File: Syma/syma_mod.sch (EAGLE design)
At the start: 6 parts, among them Q1 BSS84, Q2 BSS84, Q3 BSS84

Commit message: syma update
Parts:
- added C1: 470p, rcl:C-EUC0603
- added D1: (no value), palmquad_alpha:DIODE-MINIMELF
- added M4: MOTORARM-CORNER, palmquad_alpha:MOTORARM-CORNER
- added Q5: DMN2075U, palmquad_alpha:MOSFET-NCHANNELSMD
- added R7: 680K, rcl:R-US_R0603
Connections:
- new net GND: Q5.S, R7.1
- new net N$20: D1.A, M4.2, Q5.D
- new net N$45: C1.2, Q5.G
- new net OC3A: C1.1, R7.2
- new net VBATT: D1.C, M4.1
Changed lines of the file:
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@@
 <layer number="48" name="Document" color="7" fill="1" visible="no" active="no"/>
 <layer number="49" name="Reference" color="7" fill="1" visible="no" active="no"/>
+<layer number="50" name="dxf" color="7" fill="1" visible="no" active="no"/>
 <layer number="51" name="tDocu" color="7" fill="1" visible="no" active="no"/>
 <layer number="52" name="bDocu" color="7" fill="1" visible="no" active="no"/>
+<layer number="53" name="tGND_GNDA" color="7" fill="9" visible="no" active="no"/>
+<layer number="54" name="bGND_GNDA" color="1" fill="9" visible="no" active="no"/>
+<layer number="56" name="wert" color="7" fill="1" visible="no" active="no"/>
 <layer number="90" name="Modules" color="5" fill="1" visible="yes" active="yes"/>
 <layer number="91" name="Nets" color="2" fill="1" visible="yes" active="yes"/>
@@
 <layer number="97" name="Info" color="7" fill="1" visible="yes" active="yes"/>
 <layer number="98" name="Guide" color="6" fill="1" visible="yes" active="yes"/>
+<layer number="100" name="Muster" color="7" fill="1" visible="no" active="no"/>
+<layer number="101" name="Patch_Top" color="12" fill="4" visible="yes" active="yes"/>
+<layer number="102" name="Vscore" color="7" fill="1" visible="yes" active="yes"/>
+<layer number="103" name="tMap" color="7" fill="1" visible="yes" active="yes"/>
+<layer number="104" name="Name" color="16" fill="1" visible="yes" active="yes"/>
+<layer number="105" name="tPlate" color="7" fill="1" visible="yes" active="yes"/>
+<layer number="106" name="bPlate" color="7" fill="1" visible="yes" active="yes"/>
+<layer number="107" name="Crop" color="7" fill="1" visible="yes" active="yes"/>
+<layer number="116" name="Patch_BOT" color="9" fill="4" visible="yes" active="yes"/>
+<layer number="121" name="_tsilk" color="7" fill="1" visible="yes" active="yes"/>
+<layer number="122" name="_bsilk" color="7" fill="1" visible="yes" active="yes"/>
+<layer number="125" name="_tNames" color="7" fill="1" visible="no" active="yes"/>
+<layer number="144" name="Drill_legend" color="7" fill="1" visible="no" active="yes"/>
+<layer number="151" name="HeatSink" color="7" fill="1" visible="yes" active="yes"/>
+<layer number="200" name="200bmp" color="1" fill="10" visible="yes" active="yes"/>
+<layer number="201" name="201bmp" color="2" fill="10" visible="yes" active="yes"/>
+<layer number="202" name="202bmp" color="3" fill="10" visible="yes" active="yes"/>
+<layer number="203" name="203bmp" color="4" fill="10" visible="yes" active="yes"/>
+<layer number="204" name="204bmp" color="5" fill="10" visible="yes" active="yes"/>
+<layer number="205" name="205bmp" color="6" fill="10" visible="yes" active="yes"/>
+<layer number="206" name="206bmp" color="7" fill="10" visible="yes" active="yes"/>
+<layer number="207" name="207bmp" color="8" fill="10" visible="yes" active="yes"/>
+<layer number="208" name="208bmp" color="9" fill="10" visible="yes" active="yes"/>
+<layer number="209" name="209bmp" color="7" fill="1" visible="yes" active="yes"/>
+<layer number="210" name="210bmp" color="7" fill="1" visible="yes" active="yes"/>
+<layer number="211" name="211bmp" color="7" fill="1" visible="yes" active="yes"/>
+<layer number="212" name="212bmp" color="7" fill="1" visible="yes" active="yes"/>
+<layer number="213" name="213bmp" color="7" fill="1" visible="yes" active="yes"/>
+<layer number="214" name="214bmp" color="7" fill="1" visible="yes" active="yes"/>
+<layer number="215" name="215bmp" color="7" fill="1" visible="yes" active="yes"/>
+<layer number="216" name="216bmp" color="7" fill="1" visible="yes" active="yes"/>
+<layer number="217" name="217bmp" color="7" fill="1" visible="yes" active="yes"/>
+<layer number="218" name="218bmp" color="7" fill="1" visible="yes" active="yes"/>
+<layer number="219" name="219bmp" color="7" fill="1" visible="yes" active="yes"/>
+<layer number="220" name="220bmp" color="7" fill="1" visible="yes" active="yes"/>
+<layer number="221" name="221bmp" color="7" fill="1" visible="yes" active="yes"/>
+<layer number="222" name="222bmp" color="7" fill="1" visible="yes" active="yes"/>
+<layer number="223" name="223bmp" color="7" fill="1" visible="yes" active="yes"/>
+<layer number="224" name="224bmp" color="7" fill="1" visible="yes" active="yes"/>
+<layer number="250" name="Descript" color="3" fill="1" visible="no" active="no"/>
+<layer number="251" name="SMDround" color="12" fill="11" visible="no" active="no"/>
+<layer number="254" name="cooling" color="7" fill="1" visible="yes" active="yes"/>
 </layers>
 <schematic xreflabel="%F%N/%S.%C%R" xrefpart="/%S.%C%R">
@@
 </part>
 <part name="SUPPLY1" library="supply2" deviceset="GND" device=""/>
+<part name="M4" library="palmquad_alpha" deviceset="MOTOR" device="ARM-CORNER"/>
+<part name="Q5" library="palmquad_alpha" deviceset="MOSFET-NCHANNEL" device="SMD" value="DMN2075U"/>
+<part name="R7" library="rcl" deviceset="R-US_" device="R0603" value="680K"/>
+<part name="GND20" library="supply1" deviceset="GND" device=""/>
+<part name="SUPPLY8" library="supply2" deviceset="+5V" device="" value="Vbatt"/>
+<part name="D1" library="palmquad_alpha" deviceset="DIODE-" device="MINIMELF"/>
+<part name="C1" library="rcl" deviceset="C-EU" device="C0603" value="470p"/>
 </parts>
 <sheets>
@@
 </instance>
 <instance part="SUPPLY1" gate="GND" x="114.3" y="180.34"/>
+<instance part="M4" gate="G$1" x="83.82" y="83.82" rot="R270"/>
+<instance part="Q5" gate="G$1" x="83.82" y="66.04"/>
+<instance part="R7" gate="G$1" x="60.96" y="58.42" rot="R90"/>
+<instance part="GND20" gate="1" x="83.82" y="45.72"/>
+<instance part="SUPPLY8" gate="+5V" x="83.82" y="99.06"/>
+<instance part="D1" gate="G$1" x="91.44" y="83.82" rot="R90"/>
+<instance part="C1" gate="G$1" x="66.04" y="66.04" rot="R90"/>
 </instances>
 <busses>
@@
 <pinref part="SUPPLY1" gate="GND" pin="GND"/>
 </segment>
+<segment>
+<wire x1="83.82" y1="60.96" x2="83.82" y2="50.8" width="0.1524" layer="91"/>
+<wire x1="83.82" y1="50.8" x2="83.82" y2="48.26" width="0.1524" layer="91"/>
+<wire x1="60.96" y1="53.34" x2="60.96" y2="50.8" width="0.1524" layer="91"/>
+<wire x1="60.96" y1="50.8" x2="83.82" y2="50.8" width="0.1524" layer="91"/>
+<pinref part="Q5" gate="G$1" pin="S"/>
+<pinref part="GND20" gate="1" pin="GND"/>
+<pinref part="R7" gate="G$1" pin="1"/>
+</segment>
 </net>
 <net name="N$1" class="0">
@@
 </segment>
 </net>
+<net name="N$20" class="0">
+<segment>
+<wire x1="83.82" y1="73.66" x2="83.82" y2="71.12" width="0.1524" layer="91"/>
+<wire x1="83.82" y1="73.406" x2="83.82" y2="73.66" width="0.1524" layer="91"/>
+<wire x1="91.44" y1="81.28" x2="91.44" y2="73.406" width="0.1524" layer="91"/>
+<wire x1="91.44" y1="73.406" x2="83.82" y2="73.406" width="0.1524" layer="91"/>
+<pinref part="Q5" gate="G$1" pin="D"/>
+<pinref part="M4" gate="G$1" pin="2"/>
+<pinref part="D1" gate="G$1" pin="A"/>
+</segment>
+</net>
+<net name="OC3A" class="0">
+<segment>
+<wire x1="60.96" y1="66.04" x2="60.96" y2="63.5" width="0.1524" layer="91"/>
+<wire x1="60.96" y1="66.04" x2="50.8" y2="66.04" width="0.1524" layer="91"/>
+<wire x1="60.96" y1="66.04" x2="63.5" y2="66.04" width="0.1524" layer="91"/>
+<label x="53.34" y="66.04" size="1.778" layer="95"/>
+<pinref part="R7" gate="G$1" pin="2"/>
+<pinref part="C1" gate="G$1" pin="1"/>
+</segment>
+</net>
+<net name="VBATT" class="0">
+<segment>
+<wire x1="83.82" y1="96.52" x2="83.82" y2="94.234" width="0.1524" layer="91"/>
+<wire x1="83.82" y1="94.234" x2="83.82" y2="93.98" width="0.1524" layer="91"/>
+<wire x1="91.44" y1="86.36" x2="91.44" y2="94.234" width="0.1524" layer="91"/>
+<wire x1="91.44" y1="94.234" x2="83.82" y2="94.234" width="0.1524" layer="91"/>
+<pinref part="SUPPLY8" gate="+5V" pin="+5V"/>
+<pinref part="M4" gate="G$1" pin="1"/>
+<pinref part="D1" gate="G$1" pin="C"/>
+</segment>
+</net>
+<net name="N$45" class="0">
+<segment>
+<wire x1="71.12" y1="66.04" x2="76.2" y2="66.04" width="0.1524" layer="91"/>
+<pinref part="Q5" gate="G$1" pin="G"/>
+<pinref part="C1" gate="G$1" pin="2"/>
+</segment>
+</net>

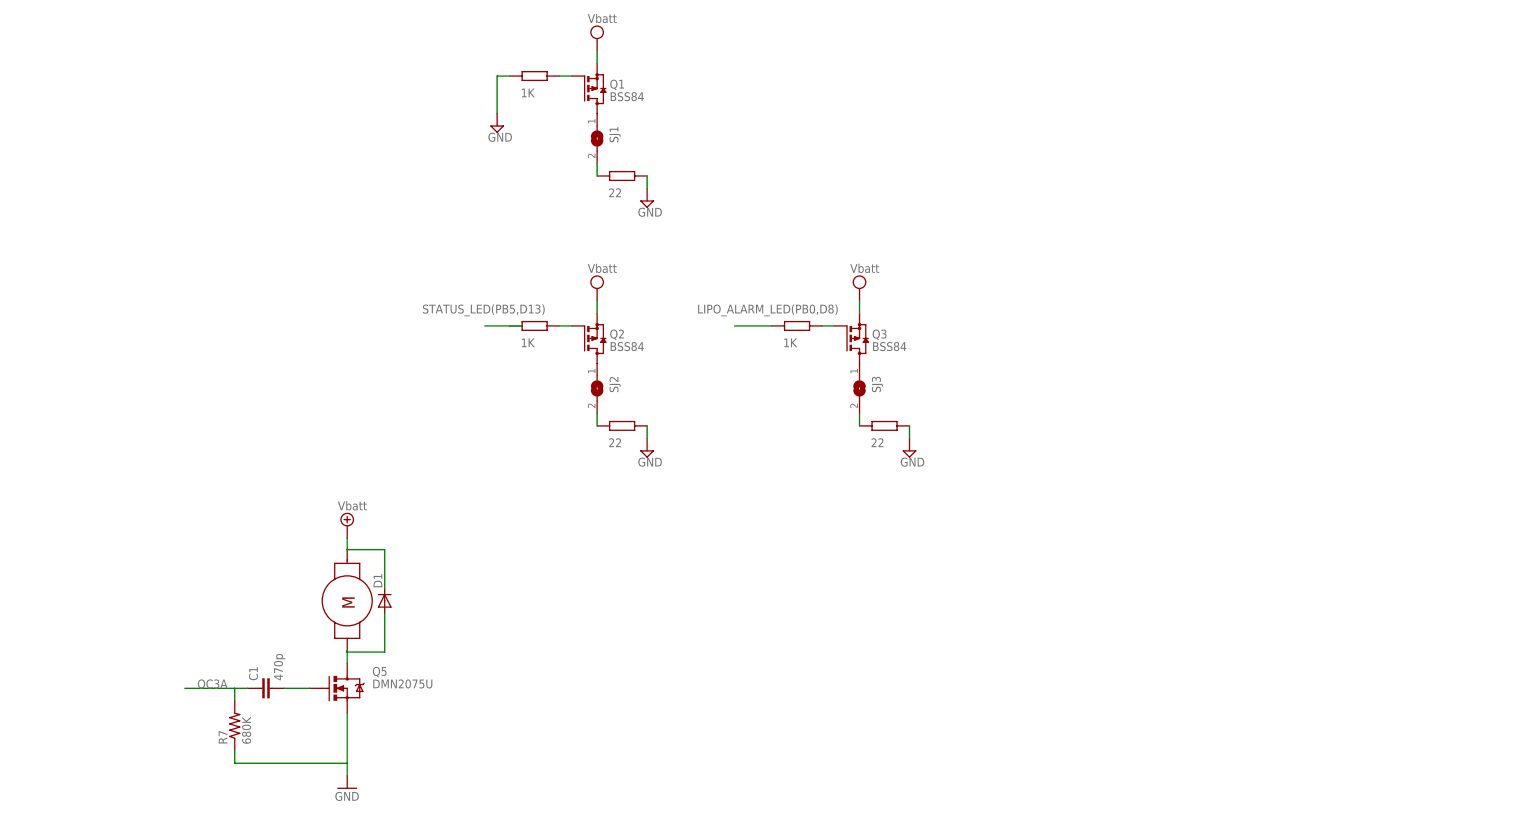
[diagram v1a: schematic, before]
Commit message: syma schematic updated
avr is added
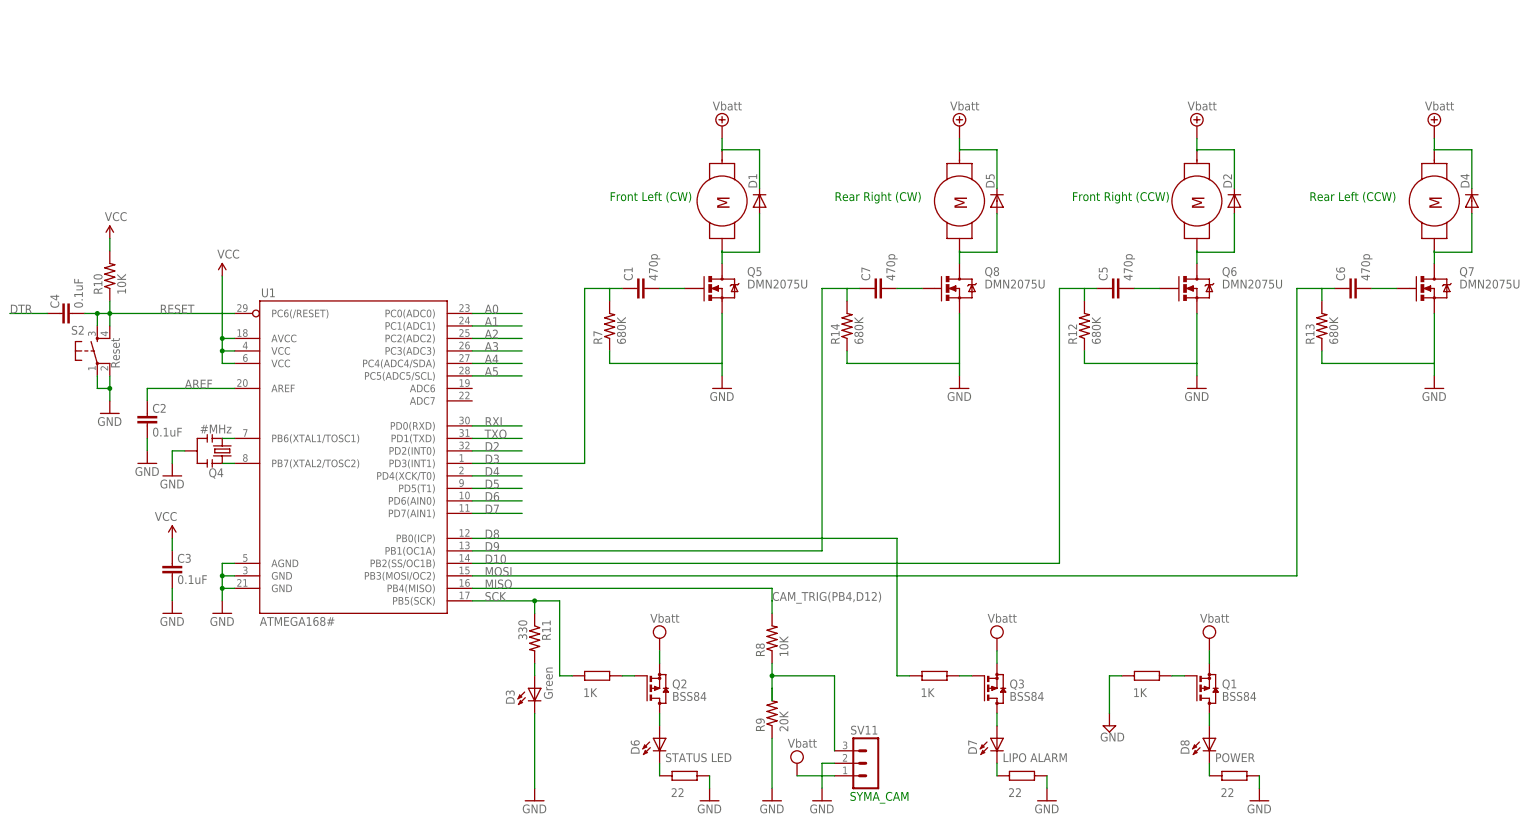
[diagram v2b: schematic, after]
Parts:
- removed SJ1, SJ2, SJ3: (no value), jumper:SJW
- added C2, C3, C4: 0.1uF, SparkFun:CAP0402
- added C5, C6, C7: 470p, rcl:C-EUC0603
- added D2, D4, D5: (no value), palmquad_alpha:DIODE-MINIMELF
- added D3: Green, SparkFun:LED0603
- added D6: STATUS LED, SparkFun:LED0603
- added D7: LIPO ALARM, SparkFun:LED0603
- added D8: POWER, SparkFun:LED0603
- added M1, M2, M3: MOTORARM-CORNER, palmquad_alpha:MOTORARM-CORNER
- added Q4: #MHz, SparkFun:RESONATORSMD
- added Q6, Q7, Q8: DMN2075U, palmquad_alpha:MOSFET-NCHANNELSMD
- added R10: 10K, SparkFun:RESISTOR0402
- added R11: 330, SparkFun:RESISTOR0402
- added R12, R13, R14: 680K, rcl:R-US_R0603
- added R8: 10K, rcl:R-US_R0603
- added R9: 20K, rcl:R-US_R0603
- added S2: Reset, SparkFun:TAC_SWITCHSND
- added SV11: (no value), con-lstb:MA03-1
- added U1: ATMEGA168#, SparkFun:ATMEGA168
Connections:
- removed net OC3A: C1.1, R7.2
- new net A0: U1.PC0(ADC0)
- new net A1: U1.PC1(ADC1)
- new net A2: U1.PC2(ADC2)
- new net A3: U1.PC3(ADC3)
- new net A4: U1.PC4(ADC4/SDA)
- new net A5: U1.PC5(ADC5/SCL)
- new net AREF: C2.2, U1.AREF
- new net CAM_TRIG(PB4,D12): R8.2
- new net D10: C5.1, R12.2, U1.PB2(SS/OC1B)
- new net D2: U1.PD2(INT0)
- new net D3: C1.1, R7.2, U1.PD3(INT1)
- new net D4: U1.PD4(XCK/T0)
- new net D5: U1.PD5(T1)
- new net D6: U1.PD6(AIN0)
- new net D7: U1.PD7(AIN1)
- new net D8: U1.PB0(ICP)
- new net D9: C7.1, R14.2, U1.PB1(OC1A)
- new net DTR: C4.2
- new net MISO: U1.PB4(MISO)
- new net MOSI: C6.1, R13.2, U1.PB3(MOSI/OC2)
- new net N$10: D3.A, R11.2
- new net N$11: Q4.1, U1.PB7(XTAL2/TOSC2)
- new net N$12: Q4.3, U1.PB6(XTAL1/TOSC1)
- new net N$13: D2.A, M1.2, Q6.D
- new net N$14: C5.2, Q6.G
- new net N$15: D4.A, M2.2, Q7.D
- new net N$16: C6.2, Q7.G
- new net N$17: D5.A, M3.2, Q8.D
- new net N$18: C7.2, Q8.G
- new net RESET: C4.1, R10.1, S2.3, S2.4, U1.PC6(/RESET)
- new net RXI: U1.PD0(RXD)
- new net SCK: R11.1, U1.PB5(SCK)
- new net SYMA_CAM_TRIG: R8.1, R9.2, SV11.3
- new net TXO: U1.PD1(TXD)
- net GND: now also C2.1, C3.1, D3.C, Q4.2, Q6.S, Q7.S, Q8.S, R12.1, R13.1, R14.1, R9.1, S2.1, S2.2, SV11.2, U1.AGND, U1.GND@1, U1.GND@2
- net N$1: now also D6.A; no longer SJ2.1
- net N$2: now also D6.C; no longer SJ2.2
- net N$4: now also D7.A; no longer SJ3.1
- net N$5: now also D7.C; no longer SJ3.2
- net N$7: now also D8.A; no longer SJ1.1
- net N$8: now also D8.C; no longer SJ1.2
- net VBATT: now also D2.C, D4.C, D5.C, M1.1, M2.1, M3.1
- net VCC: now also C3.2, R10.2, SV11.1, U1.AVCC, U1.VCC@1, U1.VCC@2
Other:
- note added: "Front Left (CW)"
- note added: "Front Right (CCW)"
- note added: "Rear Left (CCW)"
- note added: "Rear Right (CW)"
- note added: "SYMA_CAM"
- moved on the sheet: C1, D1, Q1, Q2, Q3, Q5, R7

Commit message: syma schematic - add voltage sense
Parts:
- added R15, R16: 680K, rcl:R-US_R0603
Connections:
- new net +5V: Q1.S, Q2.S, Q3.S, R15.2
- net A3: now also R15.1, R16.2
- net GND: now also R16.1
- net VCC: no longer Q1.S, Q2.S, Q3.S
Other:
- moved on the sheet: C1, C5, C6, D2, D4, D5, Q6, Q7, Q8, R12, R13, R7

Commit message: syma update
eeprom test for bit chip lcd
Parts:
- R15: value 680K -> 100
- R16: value 680K -> 1K
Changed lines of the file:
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@@
 <part name="D7" library="SparkFun" deviceset="LED" device="0603" value="LIPO ALARM"/>
 <part name="D8" library="SparkFun" deviceset="LED" device="0603" value="POWER"/>
-<part name="R15" library="rcl" deviceset="R-US_" device="R0603" value="680K"/>
-<part name="R16" library="rcl" deviceset="R-US_" device="R0603" value="680K"/>
+<part name="R15" library="rcl" deviceset="R-US_" device="R0603" value="100"/>
+<part name="R16" library="rcl" deviceset="R-US_" device="R0603" value="1K"/>
 <part name="GND15" library="supply1" deviceset="GND" device=""/>
 <part name="SUPPLY5" library="supply2" deviceset="+5V" device="" value="Vbatt"/>
